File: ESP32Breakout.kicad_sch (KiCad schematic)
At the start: 22 parts, among them J1 PIN10-13_Breakout, J3 USB_C_Receptacle_USB2.0_16P, SW1 PTS636SM43SMTR LFS, SW2 PTS636SM43SMTR LFS, U1 ESP32-S3-WROOM-1

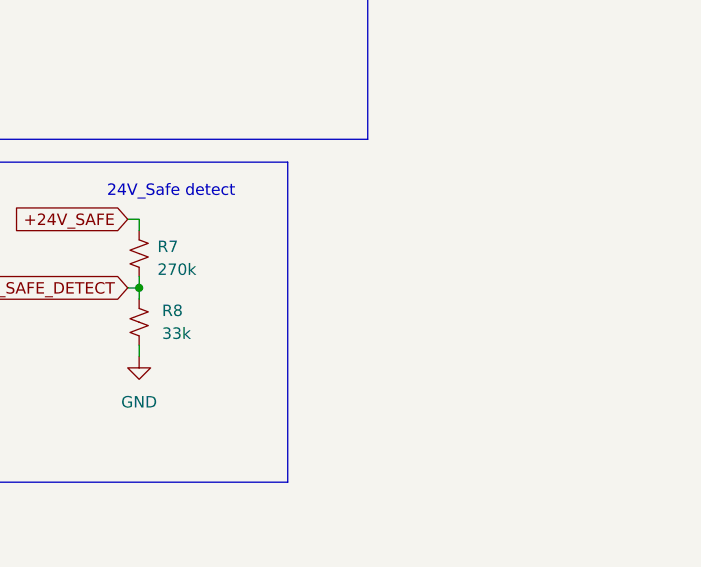
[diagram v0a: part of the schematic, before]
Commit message: minor fixed + lowered status leds to ~0.6mA, which should give ~50 mcd
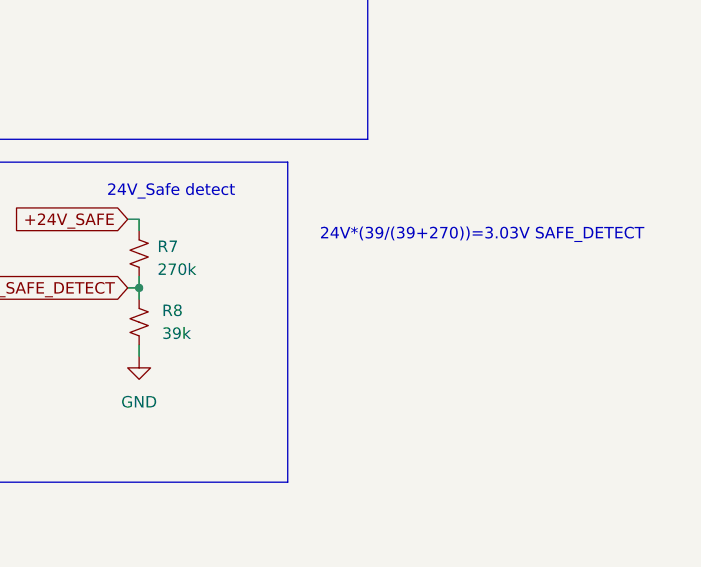
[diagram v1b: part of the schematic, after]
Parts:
- R8: value 33k -> 39k
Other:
- note added: "24V*(39/(39+270))=3.03V SAFE_DETECT"
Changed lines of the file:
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@@
+		)
+	)
+	(text "24V*(39/(39+270))=3.03V SAFE_DETECT"
+		(exclude_from_sim no)
+		(at 226.06 84.328 0)
+		(effects
+			(font
+				(size 1.27 1.27)
+			)
 		)
 	)
@@
 			)
 		)
-		(property "Value" "33k"
+		(property "Value" "39k"
 			(at 190.5 95.2499 0)
 			(effects

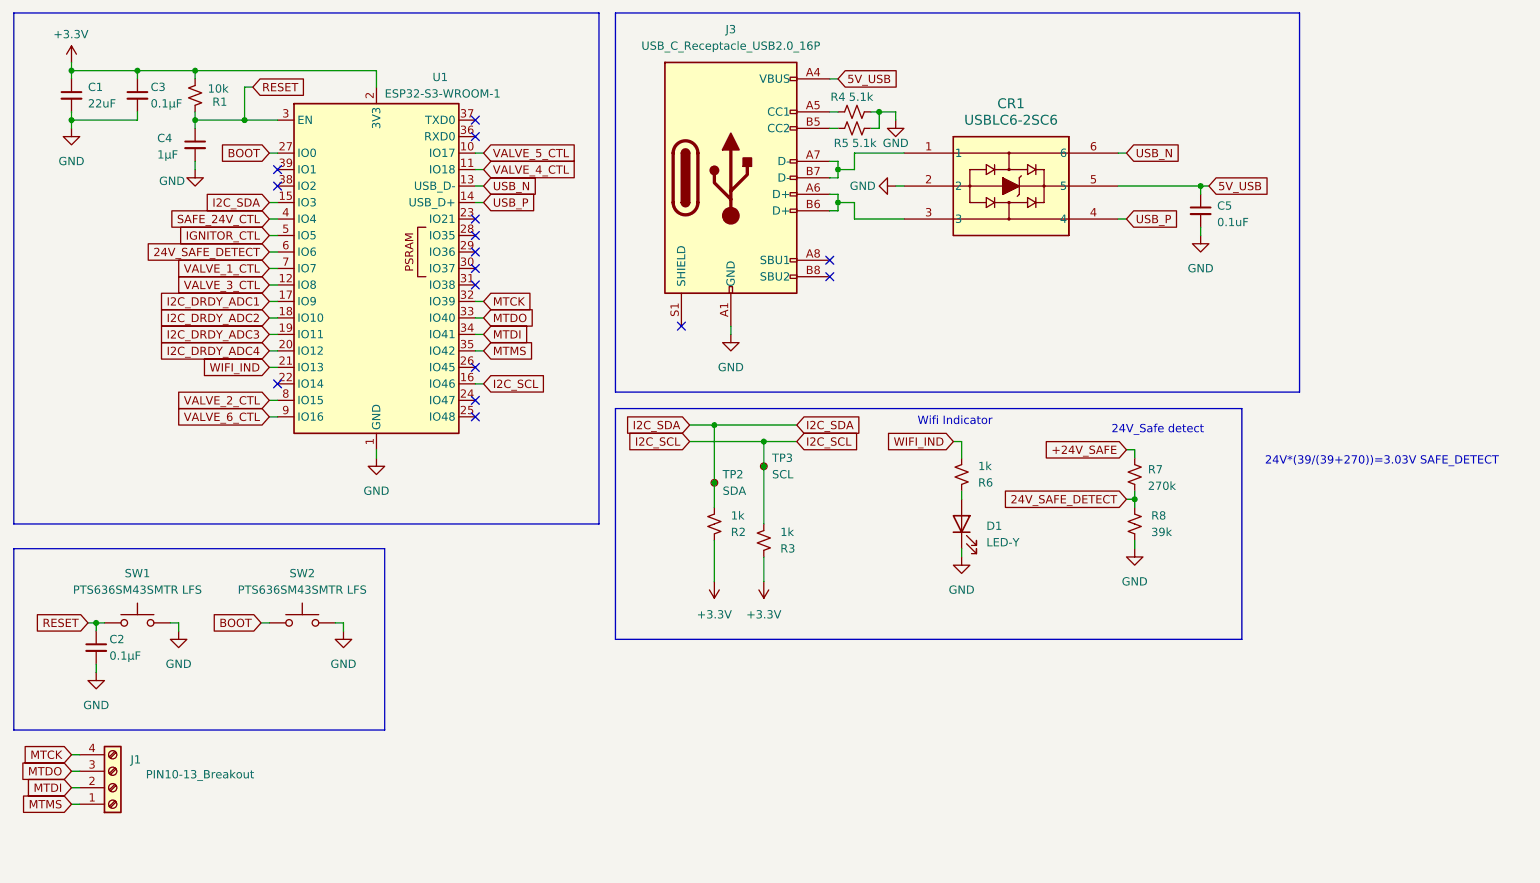
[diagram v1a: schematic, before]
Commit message: revamped schematic to be more readable
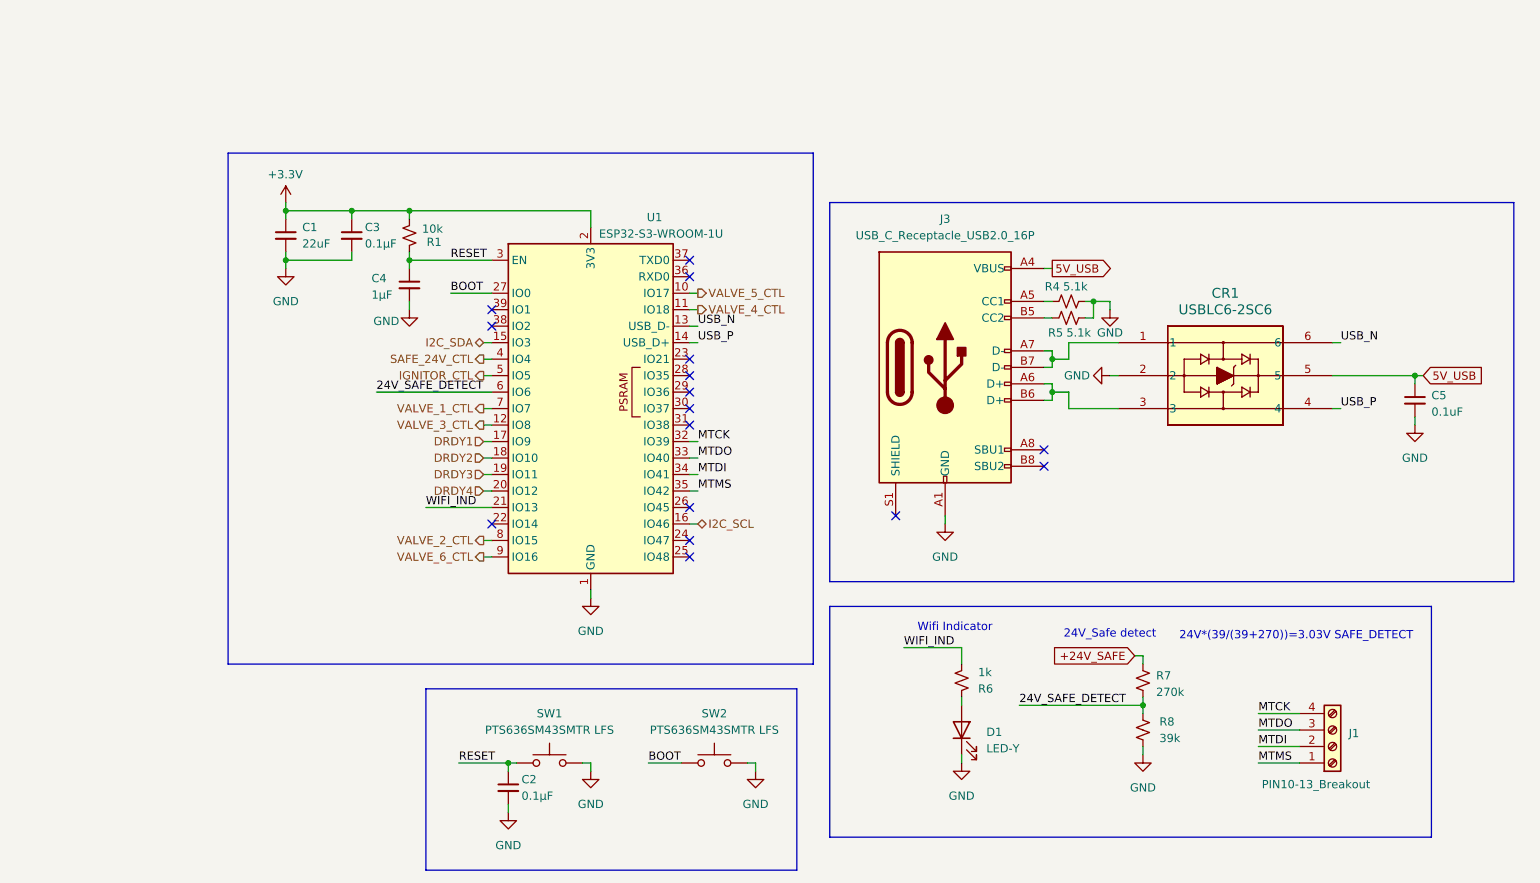
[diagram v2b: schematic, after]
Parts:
- removed R2, R3: 1k, Resistor_SMD:R_0402_1005Metric, symbol Device:R_Small_US
- removed TP2: SDA, TestPoint:TestPoint_Pad_D1.5mm, symbol Connector:TestPoint_Small
- removed TP3: SCL, TestPoint:TestPoint_Pad_D1.5mm, symbol Connector:TestPoint_Small
- U1: value ESP32-S3-WROOM-1 -> ESP32-S3-WROOM-1U
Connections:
- net I2C_DRDY_ADC1 renamed DRDY1
- net I2C_DRDY_ADC2 renamed DRDY2
- net I2C_DRDY_ADC3 renamed DRDY3
- net I2C_DRDY_ADC4 renamed DRDY4
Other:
- moved on the sheet: C1, C2, C3, C4, C5, CR1, D1, J1, J3, R1, R4, R5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

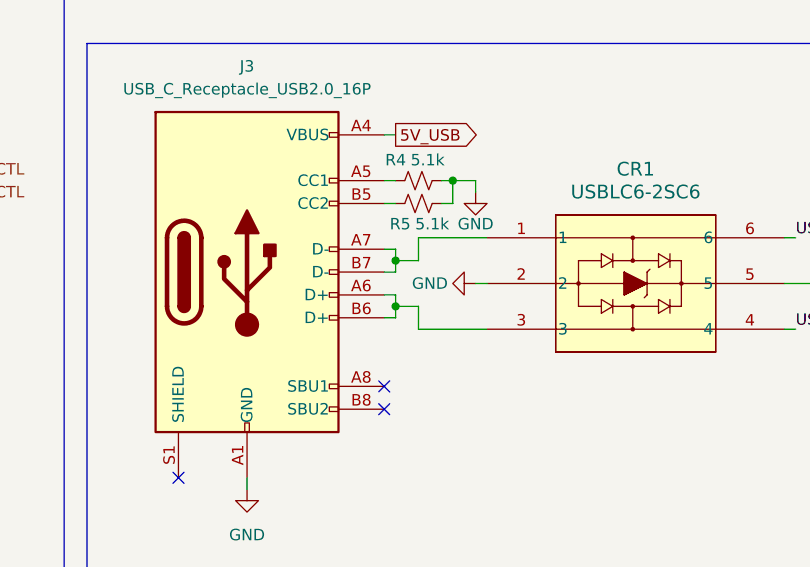
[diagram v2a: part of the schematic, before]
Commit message: remove diode between 5V and 5V_USB due to oversight (ADS112C04 cannot have DVDD without AVDD)
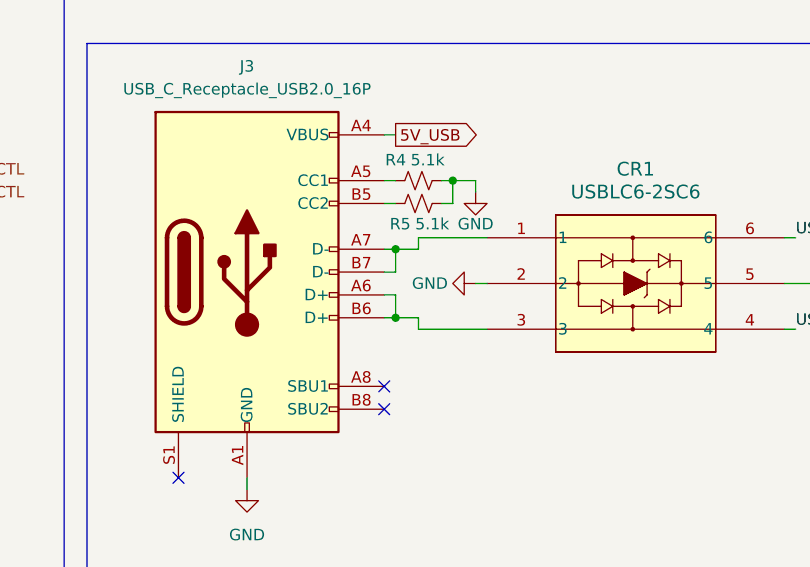
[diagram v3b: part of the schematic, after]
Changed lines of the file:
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@@
+	)
+	(junction
+		(at 175.26 74.93)
+		(diameter 0)
+		(color 0 0 0 0)
 	)
 	(junction
@@
 	)
 	(junction
-		(at 175.26 73.66)
+		(at 175.26 67.31)
 		(diameter 0)
 		(color 0 0 0 0)
@@
 	)
 	(junction
-		(at 175.26 68.58)
-		(diameter 0)
-		(color 0 0 0 0)
-	)
-	(junction
 		(at 181.61 59.69)
 		(diameter 0)
@@
 	(wire
 		(pts
-			(xy 177.8 66.04) (xy 177.8 68.58)
+			(xy 177.8 66.04) (xy 177.8 67.31)
 		)
 		(stroke
@@
 	(wire
 		(pts
-			(xy 175.26 68.58) (xy 175.26 69.85)
-		)
-		(stroke
-			(width 0)
-			(type default)
-		)
-	)
-	(wire
-		(pts
 			(xy 87.63 83.82) (xy 88.9 83.82)
 		)
@@
 	(wire
 		(pts
-			(xy 177.8 68.58) (xy 175.26 68.58)
+			(xy 177.8 67.31) (xy 175.26 67.31)
 		)
 		(stroke
@@
 	(wire
 		(pts
-			(xy 177.8 76.2) (xy 177.8 73.66)
+			(xy 177.8 76.2) (xy 177.8 74.93)
 		)
 		(stroke
@@
 	(wire
 		(pts
-			(xy 175.26 67.31) (xy 175.26 68.58)
+			(xy 175.26 67.31) (xy 175.26 69.85)
 		)
 		(stroke
@@
 	(wire
 		(pts
-			(xy 177.8 73.66) (xy 175.26 73.66)
+			(xy 177.8 74.93) (xy 175.26 74.93)
 		)
 		(stroke
@@
 	(wire
 		(pts
-			(xy 175.26 72.39) (xy 175.26 73.66)
-		)
-		(stroke
-			(width 0)
-			(type default)
-		)
-	)
-	(wire
-		(pts
 			(xy 76.2 59.69) (xy 76.2 60.96)
 		)
@@
 	(wire
 		(pts
-			(xy 175.26 73.66) (xy 175.26 74.93)
-		)
-		(stroke
+			(xy 175.26 72.39) (xy 175.26 74.93)
+		)
+		(stroke

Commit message: add power sequencing
add usb VBUS ORing
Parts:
- CR1: LCSC (none) -> C7519
- U1: LCSC (none) -> C3013946
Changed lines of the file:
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@@
+			)
+		)
+		(property "LCSC" "C7519"
+			(at 185.42 66.04 0)
+			(effects
+				(font
+					(size 1.27 1.27)
+				)
+				(hide yes)
 			)
 		)
@@
 			(at 104.14 76.2 0)
 			(effects
+				(font
+					(size 1.27 1.27)
+				)
+				(hide yes)
+			)
+		)
+		(property "LCSC" "C3013946"
+			(at 104.14 76.2 0)
+			(effects
